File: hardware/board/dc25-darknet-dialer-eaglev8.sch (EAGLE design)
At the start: 86 parts, among them SW1 RESET, X1 10118193-0001LF, Y1 RESONATORSMD

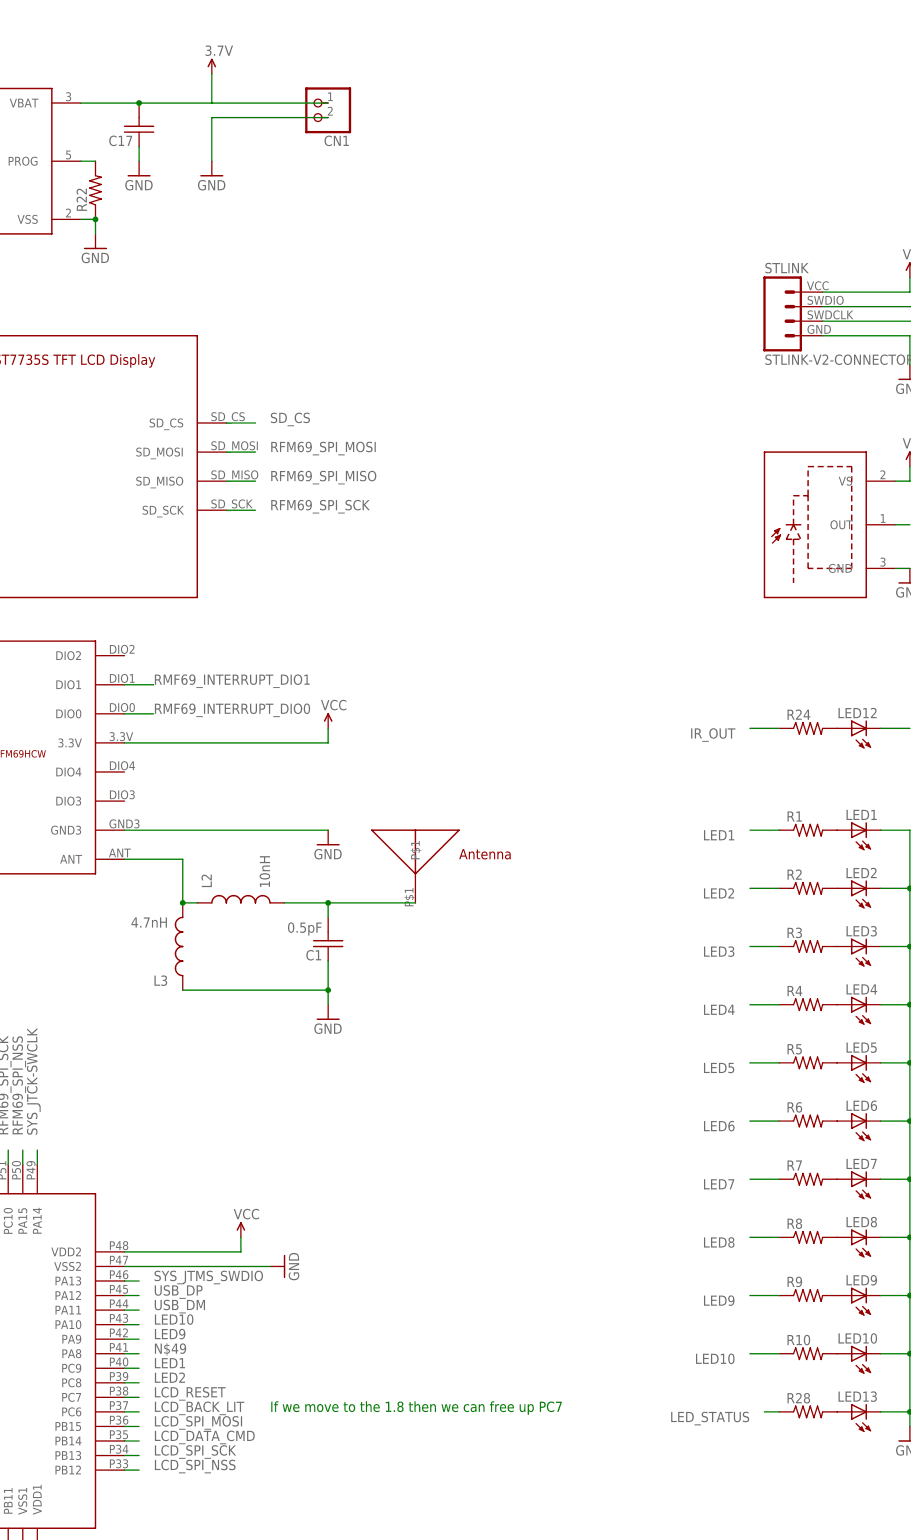
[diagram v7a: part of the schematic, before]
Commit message: Changed orientation of IR reciver
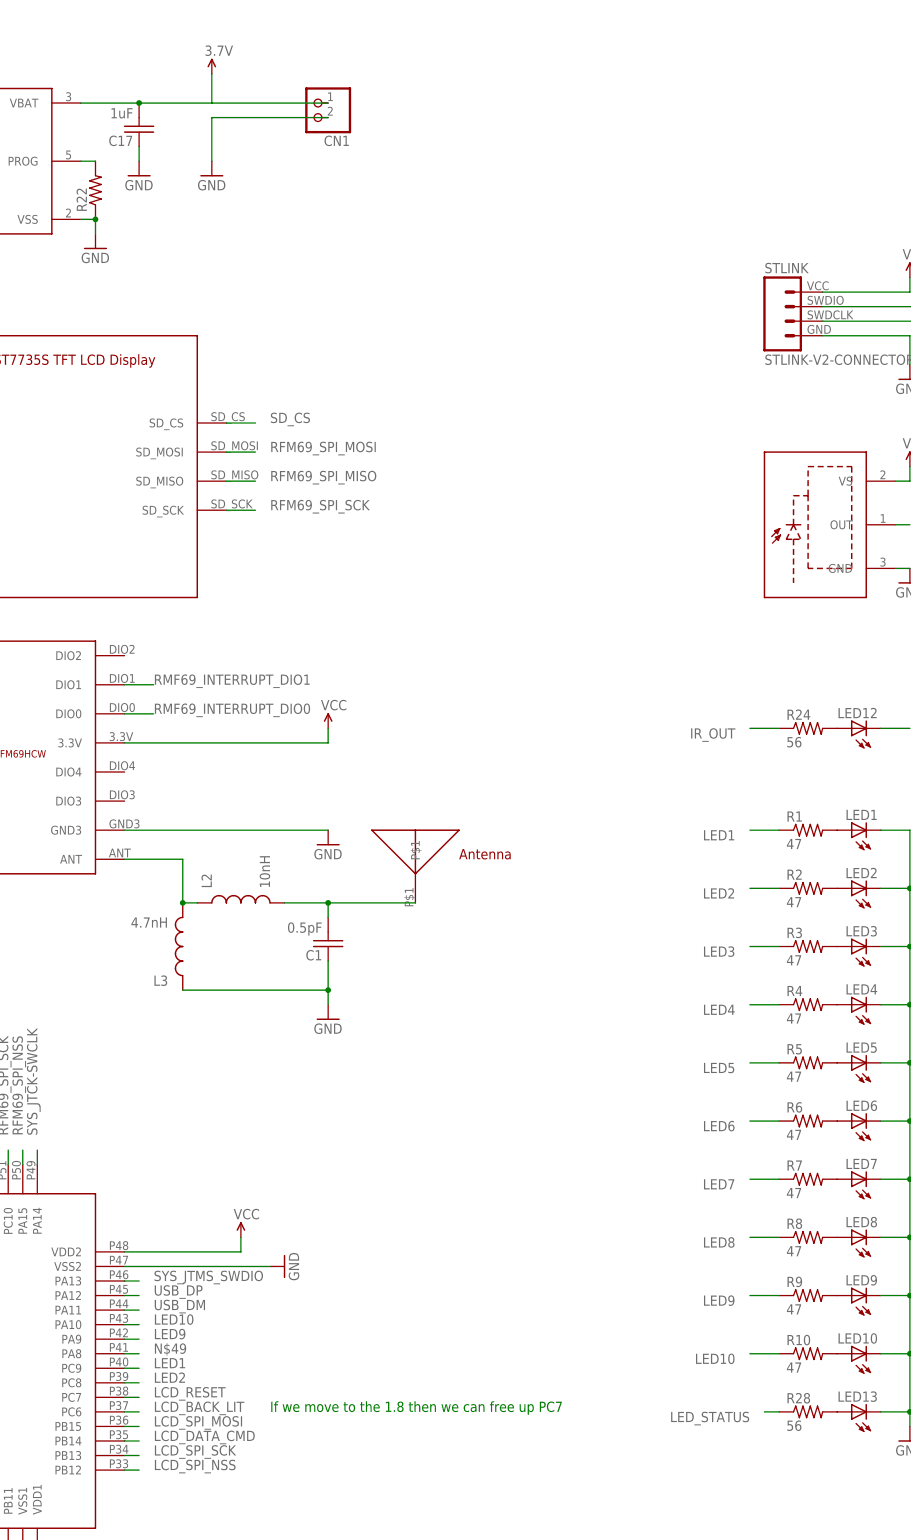
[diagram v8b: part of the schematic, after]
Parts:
- C17: value (none) -> 1uF
- R1, R10, R2, R3, R4, R5, R6, R7, R8, R9: value (none) -> 47
- R24, R28: value (none) -> 56
- U$17: value SOP22 -> SOP22FLAT; device darknet_parts_library:SOP22 -> darknet_parts_library:SOP22FLAT
